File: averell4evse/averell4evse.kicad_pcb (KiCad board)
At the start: 2 copper layers, 91 x 78 mm, 35 parts, among them J1 Conn_01x16, J2 Conn_01x12, J3 Conn_01x04, U1 KT2520K-T, U2 NFCv4, U3 TLC5957RTQ, U4 74AUC1G126, U5 touch_sensor

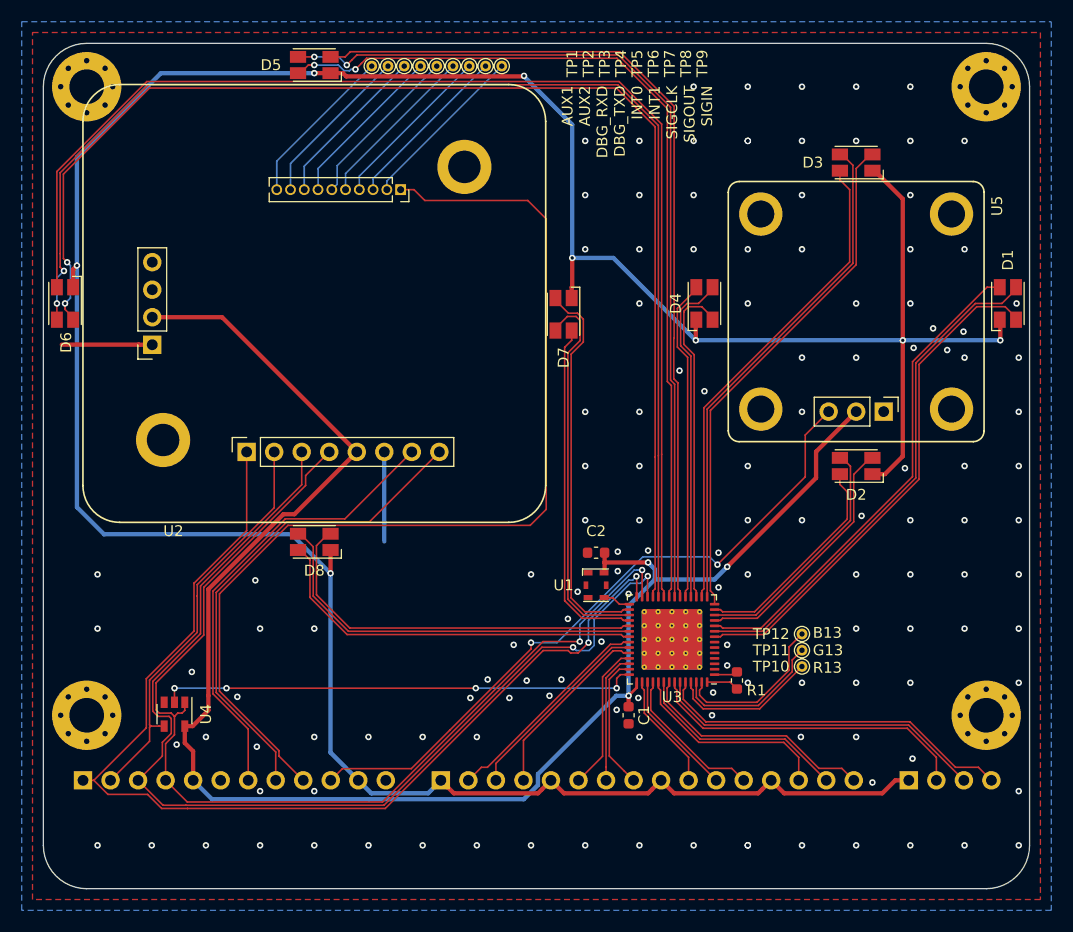
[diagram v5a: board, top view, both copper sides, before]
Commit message: averell/pcb: Add conn + copyright to silkscreen
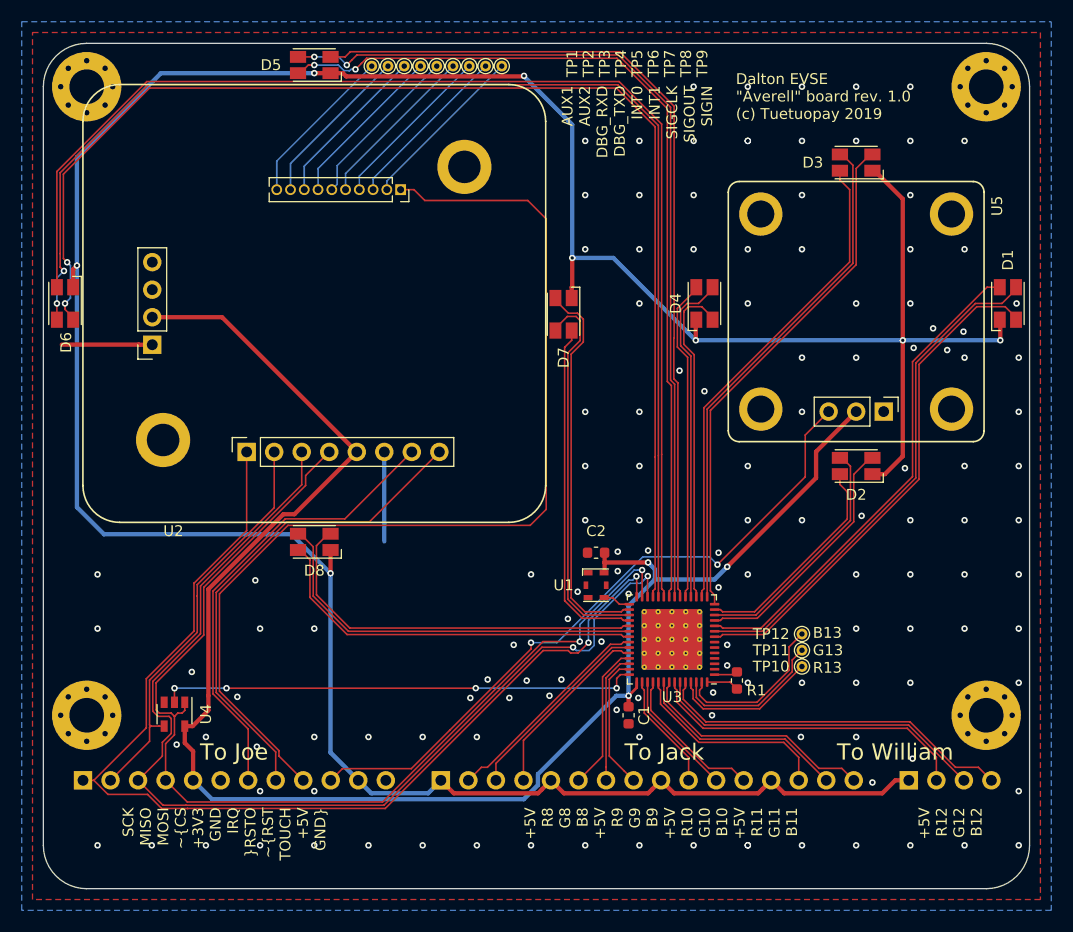
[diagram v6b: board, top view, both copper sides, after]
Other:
- board text added: "+5V R12 G12 B12"
- board text added: "+5V R8 G8 B8 +5V R9 G9 B9 +5V R10 G10 B10 +5V R11 G11 B11"
- board text added: "Dalton EVSE "Averell" board rev. 1.0 (c) Tuetuopay 2019"
- board text added: "SCK MISO MOSI ~CS +3V3 GND IRQ ~RSTO ~RST TOUCH +5V GND"
- board text added: "To Jack"
- board text added: "To Joe"
- board text added: "To William"
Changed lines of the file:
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@@
   (general
     (thickness 1.6)
-    (drawings 12)
+    (drawings 25)
     (tracks 734)
     (zones 0)
@@
     (add_net "Net-(U3-Pad7)")
   )
-  (module ma4evse:LED_Avago_PLCC4_3.2x2.8mm_CW (layer F.Cu)
-    (at 123 76 270)
-    (descr https://docs.broadcom.com/docs/AV02-4186EN)
-    (tags "LED Avago PLCC-4 ASMB-MTB0-0A3A2")
-    (attr smd)
-    (fp_text reference D7 (at 4 0 270) (layer F.SilkS)
-      (effects (font (size 1 1) (thickness 0.15)))
-    )
-    (fp_text value ASMB-MTB0-0A3A2 (at 0 2.65 270) (layer F.Fab)
-      (effects (font (size 1 1) (thickness 0.15)))
-    )
-    (fp_text user %R (at 0 0 270) (layer F.Fab)
-      (effects (font (size 0.5 0.5) (thickness 0.075)))
-    )
-    (fp_line (start -0.6 -1.4) (end -1.6 -0.4) (layer F.Fab) (width 0.1))
-    (fp_line (start -1.6 -1.4) (end -1.6 1.4) (layer F.Fab) (width 0.1))
-    (fp_line (start -1.6 1.4) (end 1.6 1.4) (layer F.Fab) (width 0.1))
-    (fp_line (start 1.6 1.4) (end 1.6 -1.4) (layer F.Fab) (width 0.1))
-    (fp_line (start 1.6 -1.4) (end -1.6 -1.4) (layer F.Fab) (width 0.1))
-    (fp_line (start -2.5 -0.7) (end -2.5 -1.5) (layer F.SilkS) (width 0.12))
-    (fp_line (start -2.500044 -1.5) (end 1.95 -1.5) (layer F.SilkS) (width 0.12))
-    (fp_line (start -1.95 1.5) (end 1.95 1.5) (layer F.SilkS) (width 0.12))
-    (fp_line (start -2.5 -1.65) (end 2.5 -1.65) (layer F.CrtYd) (width 0.05))
-    (fp_line (start -2.5 -1.65) (end -2.5 1.65) (layer F.CrtYd) (width 0.05))
-    (fp_line (start 2.5 1.65) (end 2.5 -1.65) (layer F.CrtYd) (width 0.05))
-    (fp_line (start 2.5 1.65) (end -2.5 1.65) (layer F.CrtYd) (width 0.05))
-    (fp_circle (center 0 0) (end 1.12 0) (layer F.Fab) (width 0.1))
-    (pad 1 smd rect (at -1.5 -0.75 270) (size 1.5 1.1) (layers F.Cu F.Paste F.Mask)
-      (net 6 +5V))
-    (pad 2 smd rect (at 1.5 -0.75 270) (size 1.5 1.1) (layers F.Cu F.Paste F.Mask)
-      (net 24 /B6))
-    (pad 3 smd rect (at 1.5 0.75 270) (size 1.5 1.1) (layers F.Cu F.Paste F.Mask)
-      (net 23 /G6))
-    (pad 4 smd rect (at -1.5 0.75 270) (size 1.5 1.1) (layers F.Cu F.Paste F.Mask)
-      (net 22 /R6))
-    (model ${KIPRJMOD}/../ma4evse/3d/ASMB-MTB0-0A3A2.step
-      (offset (xyz -0.75 -1.15 0))
-      (scale (xyz 1 1 1))
-      (rotate (xyz -90 0 90))
-    )
-  )
   (module ma4evse:nfc_v4_mirror locked (layer F.Cu)
     (at 100 75 180)
@@
     (pad 22 thru_hole oval (at 3.465 10.5 270) (size 1 1) (drill 0.65) (layers *.Cu *.Mask)
       (net 53 "Net-(TP1-Pad1)"))
+    (model ${KIPRJMOD}/../ma4evse/3d/nfc_v4.step
+      (offset (xyz 0 0 4.1))
+      (scale (xyz 1 1 1))
+      (rotate (xyz 0 -180 0))
+    )
+    (model ${KISYS3DMOD}/Connector_PinHeader_2.54mm.3dshapes/PinHeader_1x08_P2.54mm_Vertical.step
+      (offset (xyz 6.24 13.7 2.5))
+      (scale (xyz 1 1 1))
+      (rotate (xyz 0 -180 90))
+    )
+    (model ${KISYS3DMOD}/Connector_PinHeader_2.54mm.3dshapes/PinHeader_1x04_P2.54mm_Vertical.step
+      (offset (xyz 14.95 3.81 2.5))
+      (scale (xyz 1 1 1))
+      (rotate (xyz 0 -180 0))
+    )
+    (model ${KISYS3DMOD}/Connector_PinHeader_1.27mm.3dshapes/PinHeader_1x10_P1.27mm_Vertical.step
+      (offset (xyz -7.965 -10.5 2.5))
+      (scale (xyz 1 1 1))
+      (rotate (xyz 0 -180 -90))
+    )
+  )
+  (module ma4evse:LED_Avago_PLCC4_3.2x2.8mm_CW (layer F.Cu)
+    (at 123 76 270)
+    (descr https://docs.broadcom.com/docs/AV02-4186EN)
+    (tags "LED Avago PLCC-4 ASMB-MTB0-0A3A2")
+    (attr smd)
+    (fp_text reference D7 (at 4 0 270) (layer F.SilkS)
+      (effects (font (size 1 1) (thickness 0.15)))
+    )
+    (fp_text value ASMB-MTB0-0A3A2 (at 0 2.65 270) (layer F.Fab)
+      (effects (font (size 1 1) (thickness 0.15)))
+    )
+    (fp_text user %R (at 0 0 270) (layer F.Fab)
+      (effects (font (size 0.5 0.5) (thickness 0.075)))
+    )
+    (fp_line (start -0.6 -1.4) (end -1.6 -0.4) (layer F.Fab) (width 0.1))
+    (fp_line (start -1.6 -1.4) (end -1.6 1.4) (layer F.Fab) (width 0.1))
+    (fp_line (start -1.6 1.4) (end 1.6 1.4) (layer F.Fab) (width 0.1))
+    (fp_line (start 1.6 1.4) (end 1.6 -1.4) (layer F.Fab) (width 0.1))
+    (fp_line (start 1.6 -1.4) (end -1.6 -1.4) (layer F.Fab) (width 0.1))
+    (fp_line (start -2.5 -0.7) (end -2.5 -1.5) (layer F.SilkS) (width 0.12))
+    (fp_line (start -2.500044 -1.5) (end 1.95 -1.5) (layer F.SilkS) (width 0.12))
+    (fp_line (start -1.95 1.5) (end 1.95 1.5) (layer F.SilkS) (width 0.12))
+    (fp_line (start -2.5 -1.65) (end 2.5 -1.65) (layer F.CrtYd) (width 0.05))
+    (fp_line (start -2.5 -1.65) (end -2.5 1.65) (layer F.CrtYd) (width 0.05))
+    (fp_line (start 2.5 1.65) (end 2.5 -1.65) (layer F.CrtYd) (width 0.05))
+    (fp_line (start 2.5 1.65) (end -2.5 1.65) (layer F.CrtYd) (width 0.05))
+    (fp_circle (center 0 0) (end 1.12 0) (layer F.Fab) (width 0.1))
+    (pad 1 smd rect (at -1.5 -0.75 270) (size 1.5 1.1) (layers F.Cu F.Paste F.Mask)
+      (net 6 +5V))
+    (pad 2 smd rect (at 1.5 -0.75 270) (size 1.5 1.1) (layers F.Cu F.Paste F.Mask)
+      (net 24 /B6))
+    (pad 3 smd rect (at 1.5 0.75 270) (size 1.5 1.1) (layers F.Cu F.Paste F.Mask)
+      (net 23 /G6))
+    (pad 4 smd rect (at -1.5 0.75 270) (size 1.5 1.1) (layers F.Cu F.Paste F.Mask)
+      (net 22 /R6))
+    (model ${KIPRJMOD}/../ma4evse/3d/ASMB-MTB0-0A3A2.step
+      (offset (xyz -0.75 -1.15 0))
+      (scale (xyz 1 1 1))
+      (rotate (xyz -90 0 90))
+    )
   )
   (module ma4evse:LED_Avago_PLCC4_3.2x2.8mm_CW (layer F.Cu)
@@
     )
   )
+  (gr_text "Dalton EVSE\n\"Averell\" board rev. 1.0\n(c) Tuetuopay 2019" (at 138.9 55.9) (layer F.SilkS)
+    (effects (font (size 1 1) (thickness 0.15)) (justify left))
+  )
+  (gr_text "To William" (at 152.1 111.8) (layer B.SilkS)
+    (effects (font (size 1.5 1.5) (thickness 0.3)) (justify mirror))
+  )
+  (gr_text "To Jack" (at 132.3 111.8) (layer B.SilkS)
+    (effects (font (size 1.5 1.5) (thickness 0.3)) (justify mirror))
+  )
+  (gr_text "To Joe" (at 90.9 111.8) (layer B.SilkS)
+    (effects (font (size 1.5 1.5) (thickness 0.3)) (justify mirror))
+  )
+  (gr_text "To William" (at 153.6 116.4) (layer F.SilkS)
+    (effects (font (size 1.5 1.5) (thickness 0.3)))
+  )
+  (gr_text "To Jack" (at 132.3 116.4) (layer F.SilkS)
+    (effects (font (size 1.5 1.5) (thickness 0.3)))
+  )
+  (gr_text "To Joe" (at 92.6 116.4) (layer F.SilkS)
+    (effects (font (size 1.5 1.5) (thickness 0.3)))
+  )
+  (gr_text "+5V\nR12\nG12\nB12" (at 155.3 117.7 90) (layer B.SilkS)
+    (effects (font (size 1 1) (thickness 0.15)) (justify right mirror))
+  )
+  (gr_text "+5V\nR12\nG12\nB12" (at 158.7 121.5 90) (layer F.SilkS)
+    (effects (font (size 1 1) (thickness 0.15)) (justify right))
+  )
+  (gr_text "+5V\nR8\nG8\nB8\n+5V\nR9\nG9\nB9\n+5V\nR10\nG10\nB10\n+5V\nR11\nG11\nB11" (at 132 117.7 90) (layer B.SilkS)
+    (effects (font (size 1 1) (thickness 0.15)) (justify right mirror))
+  )
+  (gr_text "+5V\nR8\nG8\nB8\n+5V\nR9\nG9\nB9\n+5V\nR10\nG10\nB10\n+5V\nR11\nG11\nB11" (at 132 121.5 90) (layer F.SilkS)
+    (effects (font (size 1 1) (thickness 0.15)) (justify right))
+  )
+  (gr_text "SCK\nMISO\nMOSI\n~CS\n+3V3\nGND\nIRQ\n~RSTO\n~RST\nTOUCH\n+5V\nGND" (at 91.7 117.7 90) (layer B.SilkS)
+    (effects (font (size 1 1) (thickness 0.15)) (justify right mirror))
+  )
+  (gr_text "SCK\nMISO\nMOSI\n~CS\n+3V3\nGND\nIRQ\n~RSTO\n~RST\nTOUCH\n+5V\nGND" (at 91.7 121.5 90) (layer F.SilkS)
+    (effects (font (size 1 1) (thickness 0.15)) (justify right))
+  )
   (gr_text "B13\nG13\nR13" (at 149.1 107) (layer B.SilkS)
